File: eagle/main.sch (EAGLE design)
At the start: 7 parts

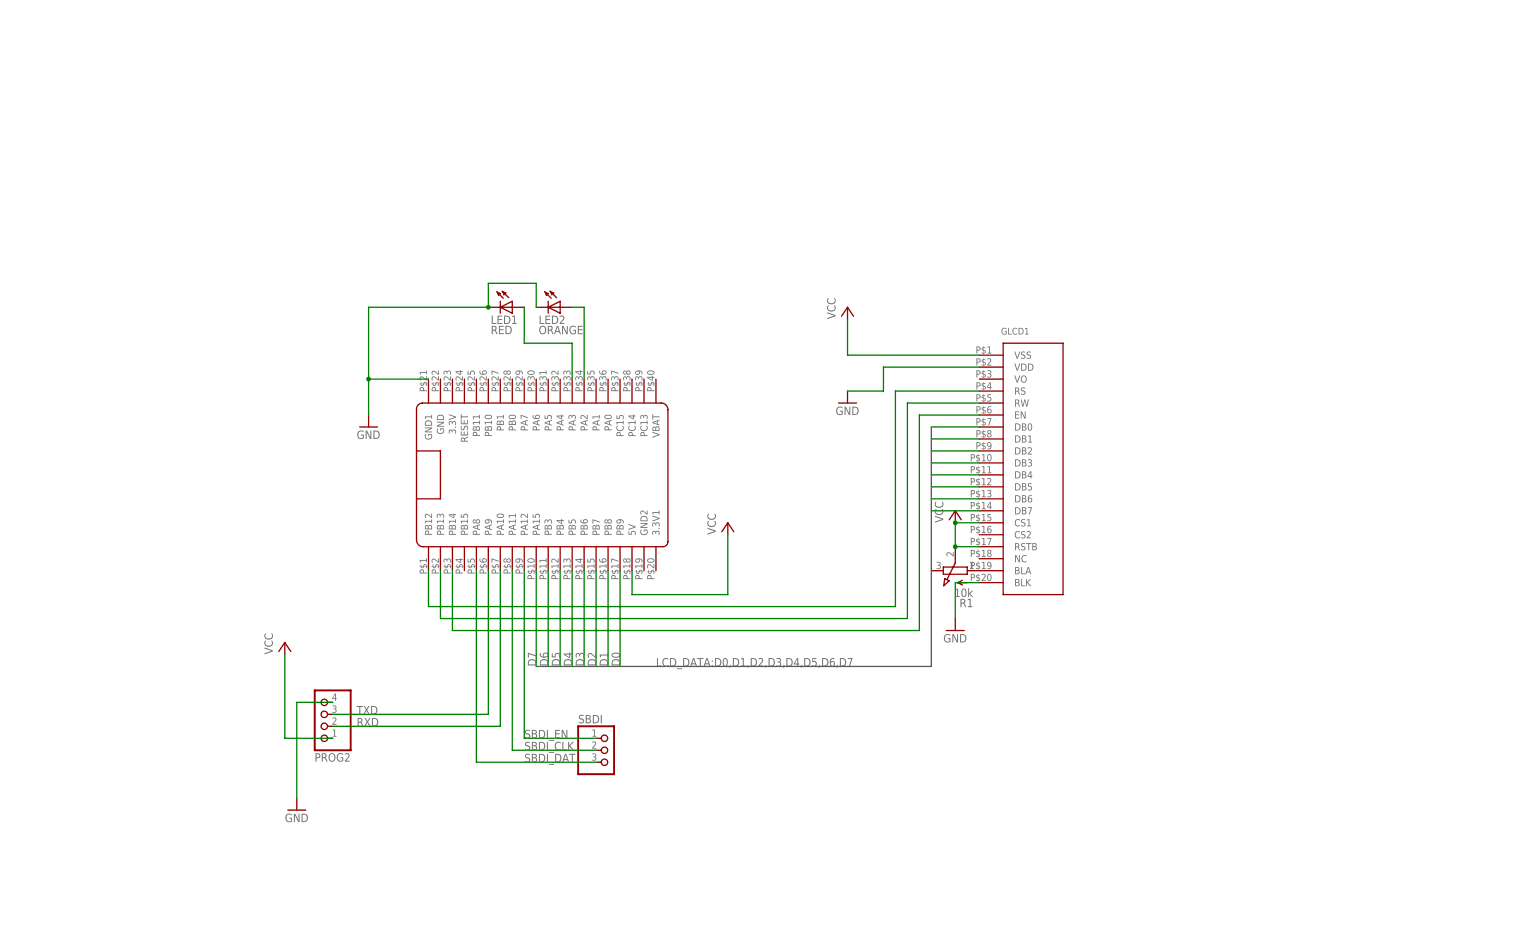
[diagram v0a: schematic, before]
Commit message: Set up part of main module schematic
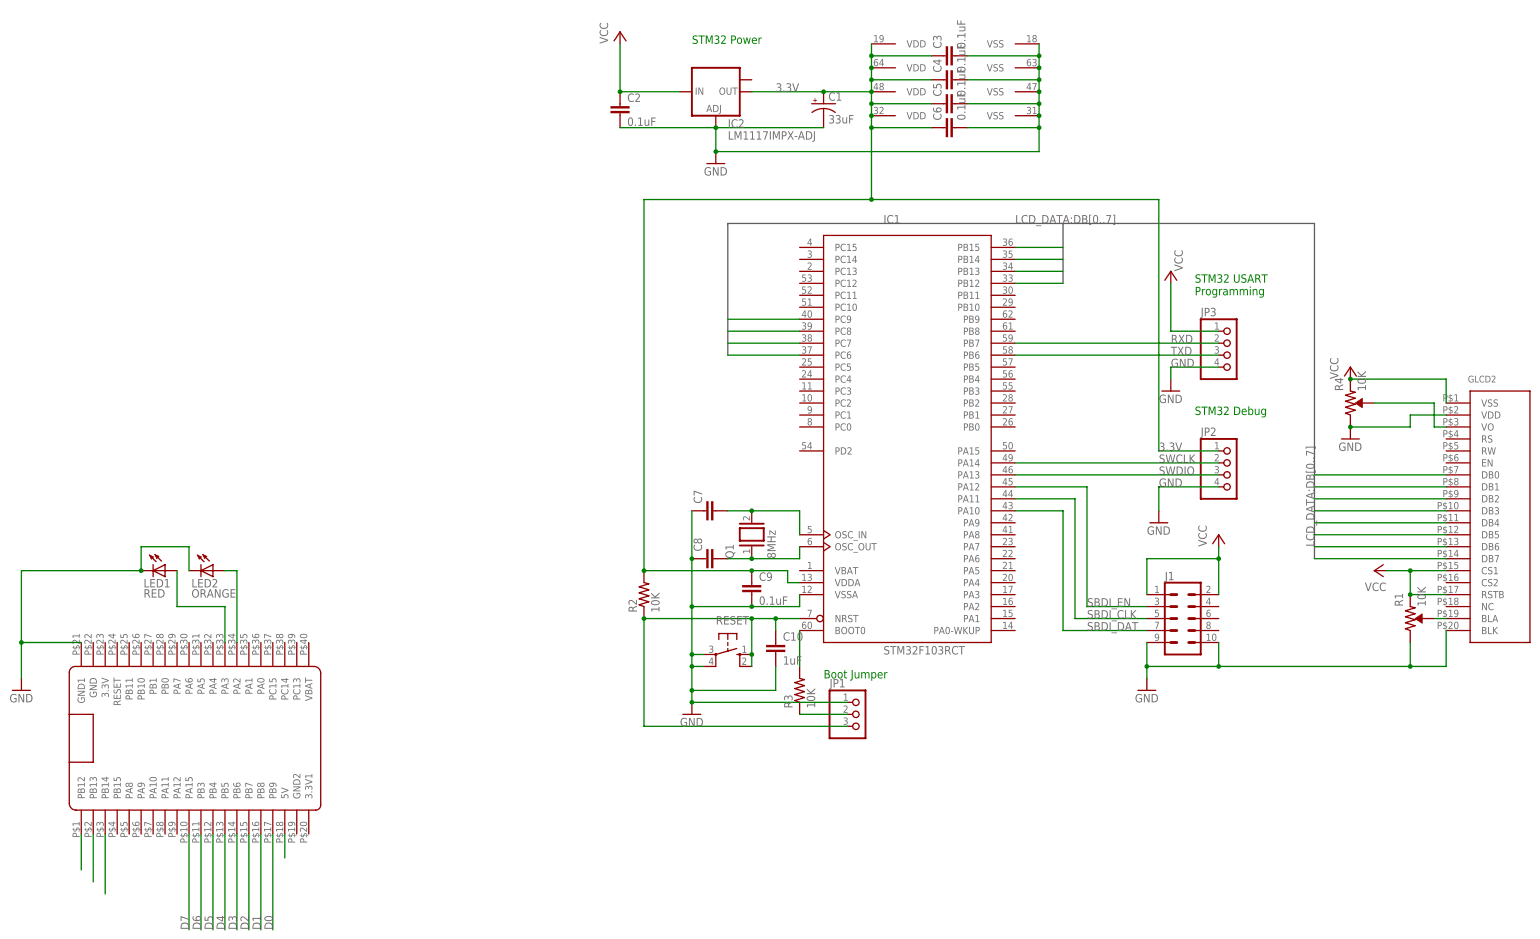
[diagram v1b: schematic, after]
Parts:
- removed GLCD1: (no value), glcd_truly_128x64_20_pines:LCD128X64
- removed PROG2: (no value), pinhead:PINHD-1X4
- removed SBDI: (no value), pinhead:PINHD-1X3
- added C1: 33uF, rcl:CPOL-USE2-5
- added C10: 1uF, rcl:C-EU025-025X050
- added C2, C3, C4, C5, C6, C9: 0.1uF, rcl:C-EU025-025X050
- added C7, C8: (no value), rcl:C-EU025-025X050
- added GLCD2: (no value), glcd_truly_128x64_20_pines:LCD128X64
- added IC1: STM32F103RCT, micro-stm_v3:STM32F103RCT
- added IC2: LM1117IMPX-ADJ, lm1117:LM1117IMPX-ADJ
- added J1: (no value), SparkFun-Connectors:CONN_05X2SHD_LOCK
- added JP1: (no value), pinhead:PINHD-1X3
- added JP2, JP3: (no value), pinhead:PINHD-1X4
- added Q1: 8MHz, special:XTAL
- added R2, R3: 10K, rcl:R-US_0204/7
- added R4: 10K, TCalc:TRIMPOT-KNOB
- added RESET: (no value), switch-omron:10-XX
- R1: value 10k -> 10K; device pot:3RP/1610N -> TCalc:TRIMPOT-KNOB
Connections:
- removed net N$2: GLCD1.RS, U$1.PB12
- removed net N$3: GLCD1.RW, U$1.PB13
- removed net N$4: GLCD1.EN, U$1.PB14
- new net 3.3V: C1.+, C3.1, C4.1, C5.1, C6.1, C9.1, IC1MCU.VDDA, IC1PWR.VDD@1, IC1PWR.VDD@2, IC1PWR.VDD@3, IC1PWR.VDD@4, IC2.OUT, JP2.1, R2.2
- new net DB0: GLCD2.DB0, IC1MCU.PC9
- new net DB1: GLCD2.DB1, IC1MCU.PC8
- new net DB2: GLCD2.DB2, IC1MCU.PC7
- new net DB3: GLCD2.DB3, IC1MCU.PC6
- new net DB4: GLCD2.DB4, IC1MCU.PB15
- new net DB5: GLCD2.DB5, IC1MCU.PB14
- new net DB6: GLCD2.DB6, IC1MCU.PB13
- new net DB7: GLCD2.DB7, IC1MCU.PB12
- new net N$10: IC1MCU.BOOT0, R3.2
- new net N$11: JP1.2, R3.1
- new net N$12: U$1.5V
- new net N$17: U$1.PB12
- new net N$18: U$1.PB13
- new net N$19: U$1.PB14
- new net N$5: C7.2, IC1MCU.OSC_IN, Q1.2
- new net N$6: C10.1, IC1MCU.NRST, JP1.3, R2.1, RESET.S, RESET.S1
- new net N$7: C8.2, IC1MCU.OSC_OUT, Q1.1
- new net N$9: GLCD2.VO, R4.2
- new net SWCLK: IC1MCU.PA14, JP2.2
- new net SWDIO: IC1MCU.PA13, JP2.3
- net D0: no longer GLCD1.DB0
- net D1: no longer GLCD1.DB1
- net D2: no longer GLCD1.DB2
- net D3: no longer GLCD1.DB3
- net D4: no longer GLCD1.DB4
- net D5: no longer GLCD1.DB5
- net D6: no longer GLCD1.DB6
- net D7: no longer GLCD1.DB7
- net GND: now also C1.-, C10.2, C2.2, C3.2, C4.2, C5.2, C6.2, C7.1, C8.1, C9.2, GLCD2.BLK, GLCD2.VDD, IC1MCU.VSSA, IC1PWR.VSS@1, IC1PWR.VSS@2, IC1PWR.VSS@3, IC1PWR.VSS@4, IC2.ADJ, J1.10, J1.9, JP1.1, JP2.4, JP3.4, R1.1, R4.1, RESET.P, RESET.P1; no longer GLCD1.BLK, GLCD1.VDD, PROG2.4
- net N$1: now also GLCD2.BLA, R1.2; no longer GLCD1.BLA, R1.A
- net RXD: now also IC1MCU.PB7, JP3.2; no longer PROG2.2, U$1.PA10
- net SBDI_CLK: now also IC1MCU.PA11, J1.5; no longer SBDI.2, U$1.PA11
- net SBDI_DAT: now also IC1MCU.PA10, J1.7; no longer SBDI.3, U$1.PA8
- net SBDI_EN: now also IC1MCU.PA12, J1.3; no longer SBDI.1, U$1.PA12
- net TXD: now also IC1MCU.PB6, JP3.3; no longer PROG2.3, U$1.PA9
- net VCC: now also C2.1, GLCD2.CS1, GLCD2.RSTB, GLCD2.VSS, IC2.IN, J1.1, J1.2, JP3.1, R1.3, R4.3; no longer GLCD1.CS1, GLCD1.RSTB, GLCD1.VSS, PROG2.1, R1.S, U$1.5V
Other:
- note added: "Boot Jumper"
- note added: "STM32 Debug"
- note added: "STM32 Power"
- note added: "STM32 USART Programming"
- moved on the sheet: LED1, LED2

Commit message: Update more of new schematic
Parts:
- Q1: device special:XTAL -> special:XTAL/S
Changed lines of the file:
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@@
 <part name="C5" library="rcl" library_urn="urn:adsk.eagle:library:334" deviceset="C-EU" device="025-025X050" package3d_urn="urn:adsk.eagle:package:23629/2" value="0.1uF"/>
 <part name="C6" library="rcl" library_urn="urn:adsk.eagle:library:334" deviceset="C-EU" device="025-025X050" package3d_urn="urn:adsk.eagle:package:23629/2" value="0.1uF"/>
-<part name="Q1" library="special" library_urn="urn:adsk.eagle:library:367" deviceset="XTAL" device="" package3d_urn="urn:adsk.eagle:package:26649/1" value="8MHz"/>
+<part name="Q1" library="special" library_urn="urn:adsk.eagle:library:367" deviceset="XTAL/S" device="" package3d_urn="urn:adsk.eagle:package:26647/2" value="8MHz"/>
 <part name="C7" library="rcl" library_urn="urn:adsk.eagle:library:334" deviceset="C-EU" device="025-025X050" package3d_urn="urn:adsk.eagle:package:23629/2"/>
 <part name="C8" library="rcl" library_urn="urn:adsk.eagle:library:334" deviceset="C-EU" device="025-025X050" package3d_urn="urn:adsk.eagle:package:23629/2"/>

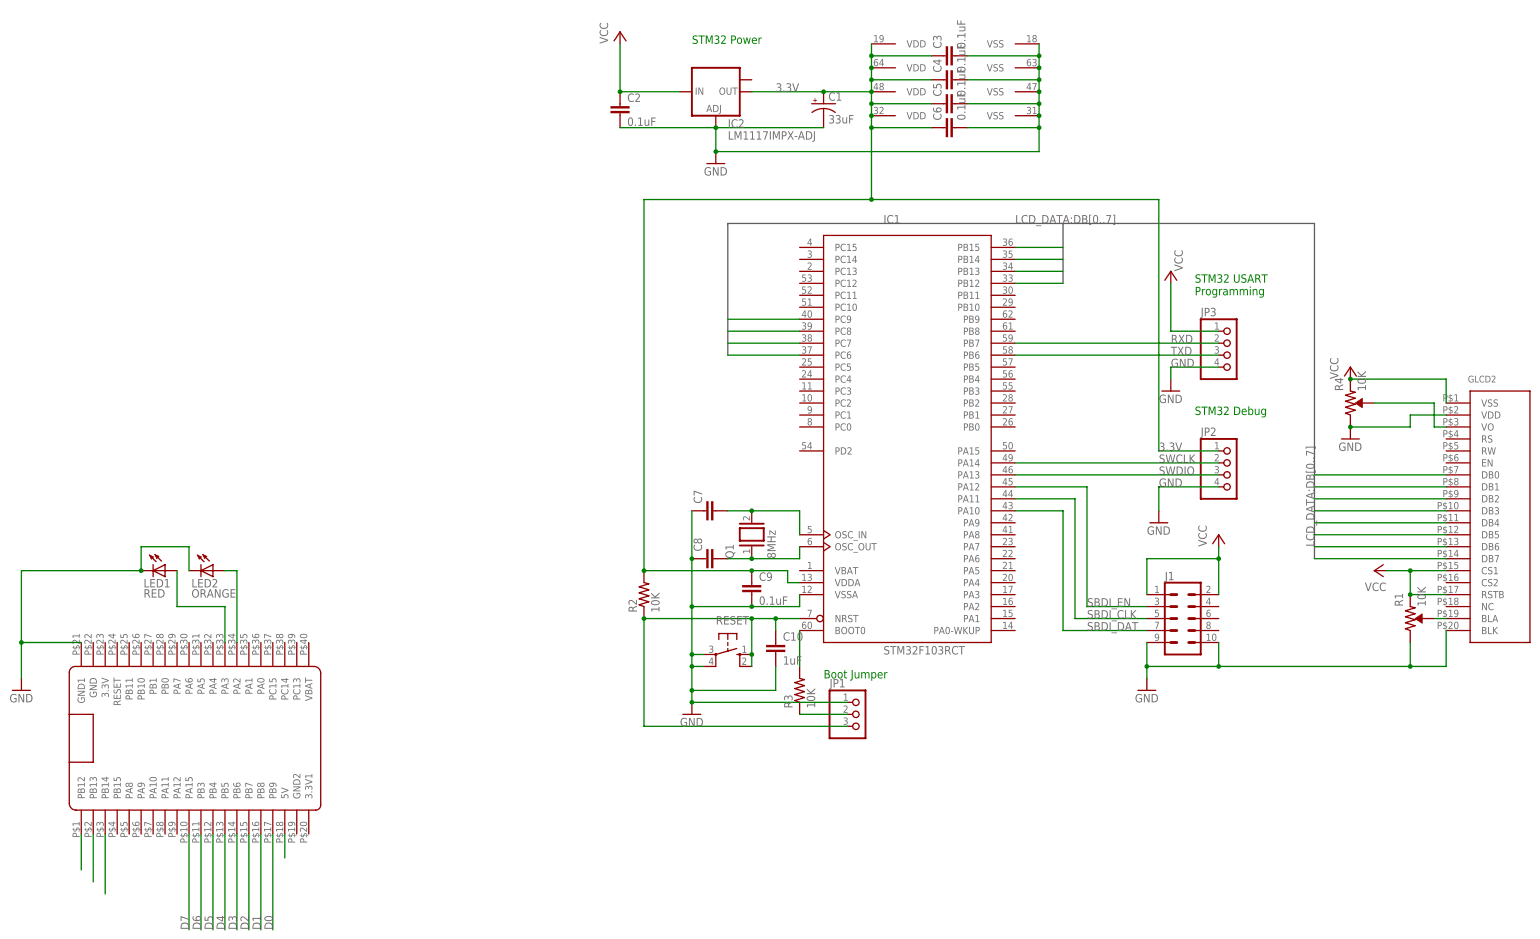
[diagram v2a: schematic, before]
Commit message: Finish basic schematic for main board
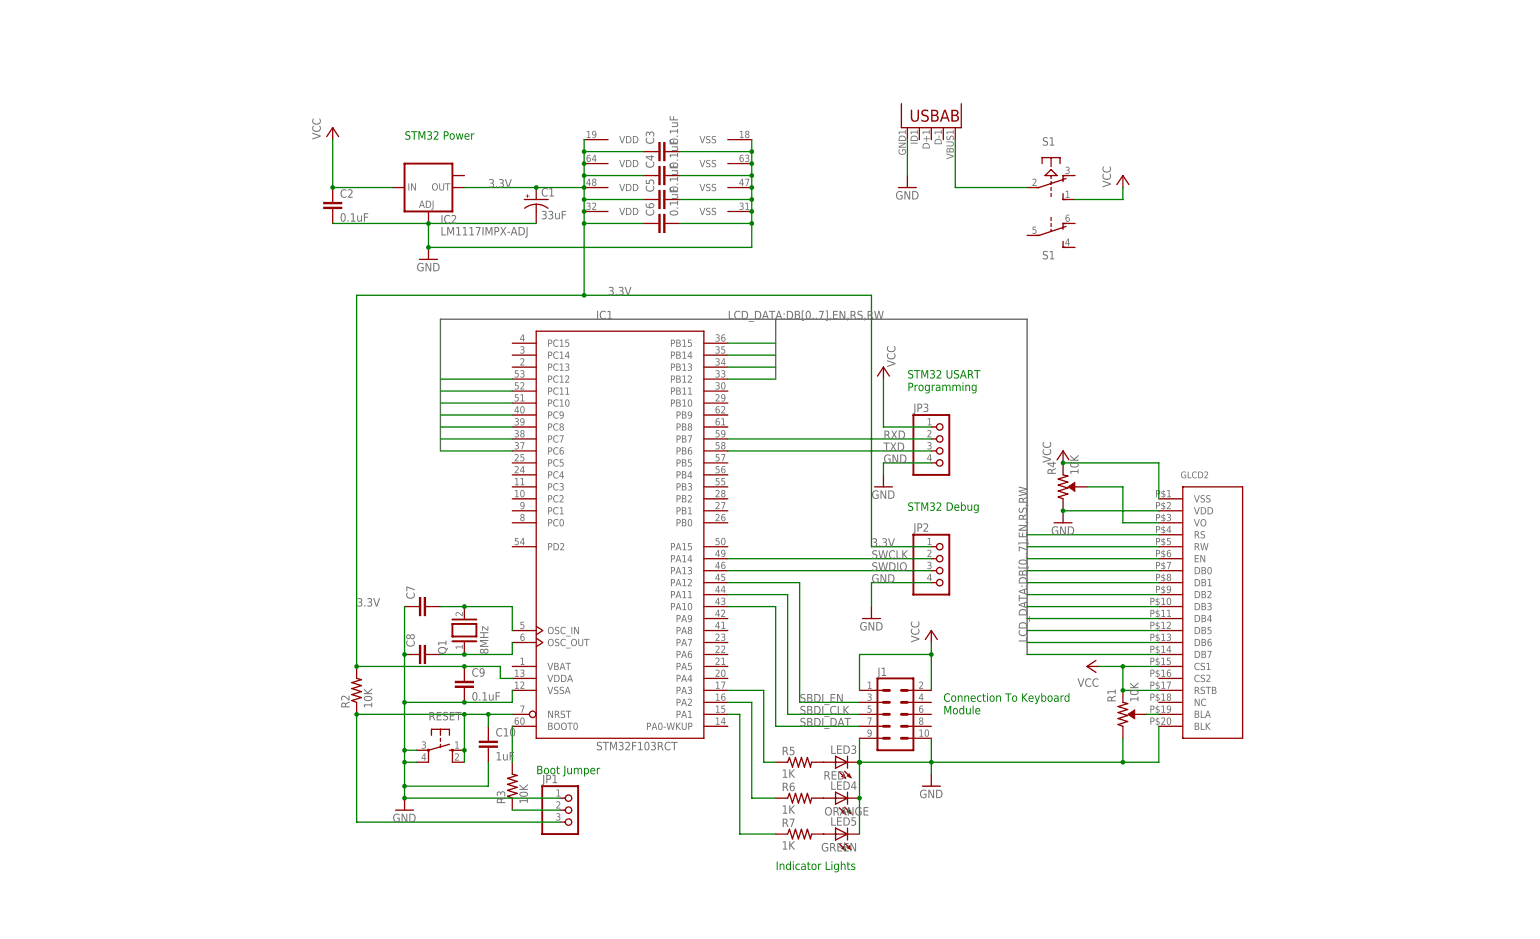
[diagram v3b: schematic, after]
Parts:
- removed LED1: RED, eagle-ltspice:LED_ELD260
- removed LED2: ORANGE, eagle-ltspice:LED_ELD260
- removed U$1: (no value), BluePill:BLUE_PILL
- added LED3: RED, led:LED5MM
- added LED4: ORANGE, led:LED5MM
- added LED5: GREEN, led:LED5MM
- added R5, R6, R7: 1K, rcl:R-US_0204/7
- added S1: PVA2R, switch-misc:PVA2R
- added U1: (no value), MicroUSB:USB""
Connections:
- removed net D0: U$1.PB9
- removed net D1: U$1.PB8
- removed net D2: U$1.PB7
- removed net D3: U$1.PB6
- removed net D4: U$1.PB5
- removed net D5: U$1.PB4
- removed net D6: U$1.PB3
- removed net D7: U$1.PA15
- removed net N$12: U$1.5V
- removed net N$17: U$1.PB12
- removed net N$18: U$1.PB13
- removed net N$19: U$1.PB14
- new net EN: GLCD2.EN, IC1MCU.PC12
- new net N$13: IC1MCU.PA2, R6.1
- new net N$14: IC1MCU.PA3, R5.1
- new net N$15: LED5.A, R7.2
- new net N$3: LED3.A, R5.2
- new net N$4: LED4.A, R6.2
- new net N$9: IC1MCU.PA1, R7.1
- new net RS: GLCD2.RS, IC1MCU.PC10
- new net RW: GLCD2.RW, IC1MCU.PC11
- net GND: now also LED3.C, LED4.C, LED5.C, U1.GND; no longer LED1.C, LED2.A, LED2.C, U$1.GND1, U$1.PA2
- net N$8: now also S11.P, U1.VBUS; no longer LED1.A, U$1.PA3
- net VCC: now also S11.S
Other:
- note added: "Connection To Keyboard Module"
- note added: "Indicator Lights"
- moved on the sheet: C1, C10, C2, C3, C4, C5, C6, C7, C8, C9, GLCD2, IC1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
